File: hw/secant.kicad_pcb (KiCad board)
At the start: 2 copper layers, 70.1 x 45.8 mm, 53 parts, among them P1 USB, P2 BUS1, P3 BUS2, P4 JTAG, P5 UART, U1 TLV70033QDDCRQ1, U2 TM4C123GE6PMI, U3 NCV7356, U4 NCV7356, U5 TJA1051T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

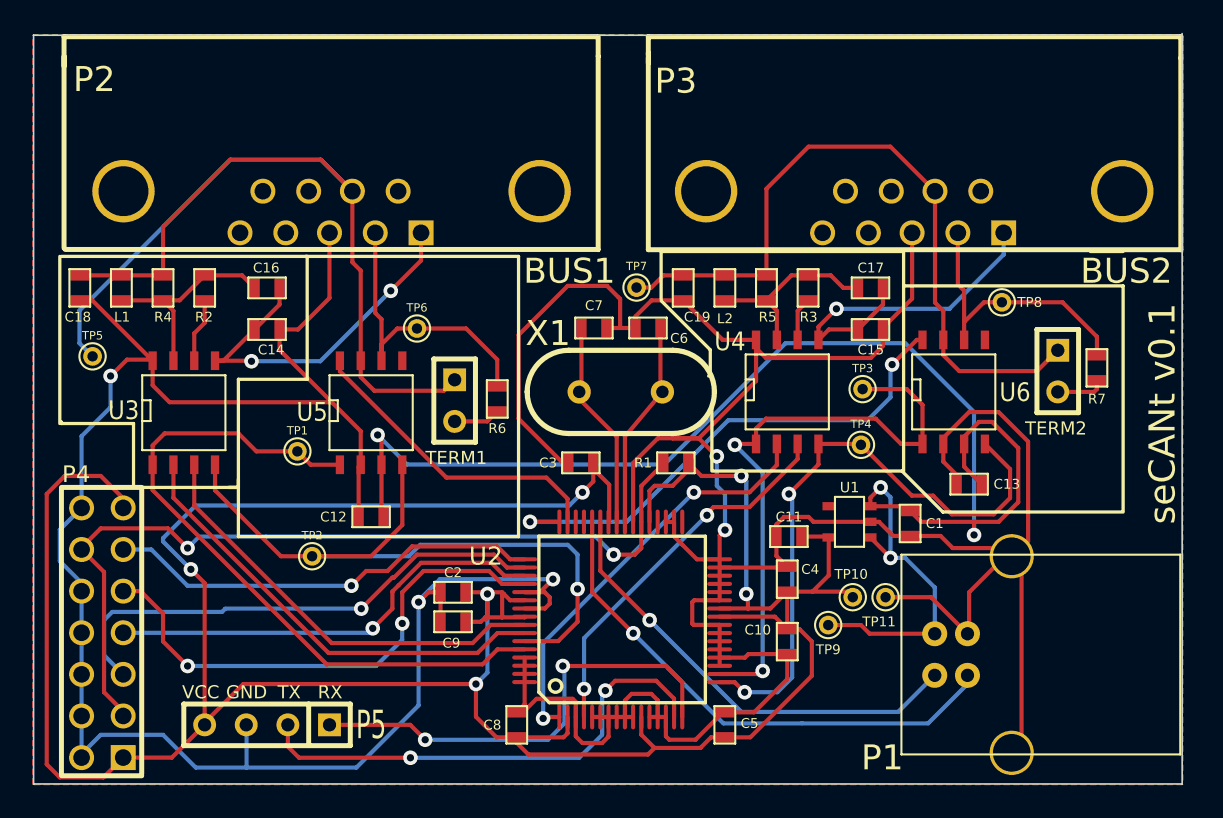
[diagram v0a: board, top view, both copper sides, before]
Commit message: fixed U2 LDO pins
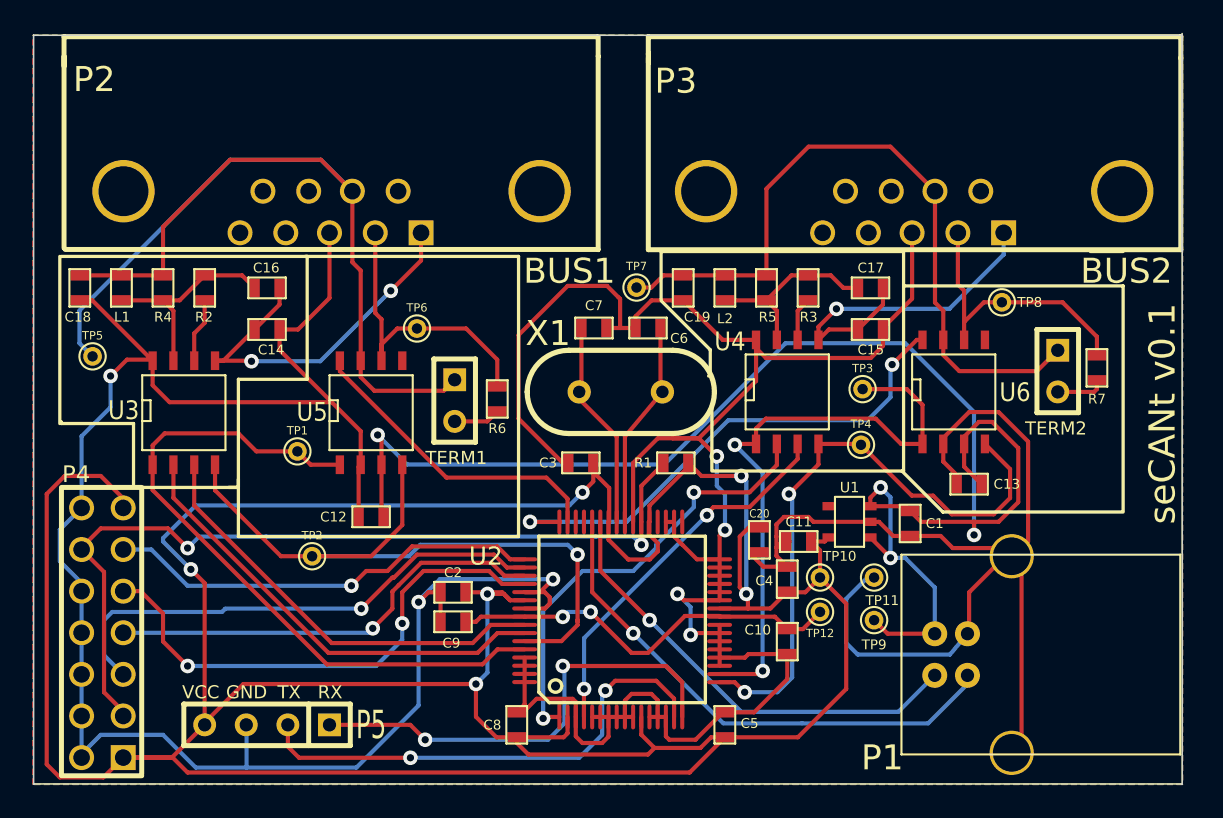
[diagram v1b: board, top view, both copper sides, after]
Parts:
- added C20: 0.1uF, SM0603, F.Cu at (201.5, 150.0)
- added TP12: TST, PINTST, F.Cu at (205.2, 154.4)
- C10, C12, C13, C2, C3, C4, C5: value C -> 0.1uF
- C8: value C -> 1uF
- C9: value C -> 2.2uF
- moved TP9 2.82 mm to (208.5, 154.9)
- moved TP10 2.33 mm to (205.2, 152.3)
- moved TP11 1.39 mm to (208.5, 152.3)
- moved C11 0.67 mm to (203.9, 150.1)
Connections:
- C10 pad 1: +3.3V -> +1.2V
- C9 pad 1: +3.3V -> +1.2V
- U2 pad 25: +3.3V -> +1.2V
- U2 pad 56: +3.3V -> +1.2V
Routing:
- net +3.3V: track 187.7 -> 226.5 mm
- net +1.2V: track 0.00 -> 24.7 mm, vias 0 -> 2
- net GND: track 305.4 -> 314.8 mm, vias 5 -> 7
- net +5V: track 97.2 -> 94.6 mm
- net /CAN1MODE0: track 25.7 -> 27.6 mm
